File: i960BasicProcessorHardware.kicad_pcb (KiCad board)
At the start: 4 copper layers, 169.9 x 169.8 mm, 76 parts, among them J1 Conn_01x08, J10 Conn_02x39_Odd_Even, J11 Conn_01x03, J12 Conn_01x03, J13 AVR-ISP-6, J14 Conn_01x06 (Serial Connector), J15 Conn_01x01, J16 Conn_01x01, J2 Conn_02x05_Odd_Even, J3 Conn_02x05_Odd_Even, J4 Conn_02x05_Odd_Even, J5 Conn_02x16_Odd_Even, J6 Conn_01x03, J7 Conn_01x03, J8 Conn_01x06, J9 Conn_01x11, U1 74HC245, U10 Adafruit_FeatherWing (PSRAM F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, U11 Adafruit_FeatherWing (PSRAM F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, U12 74LS125, U13 74LS04, U14 74LS08, U15 74LS174, U16 SN74LVC245AN, U17 74LS174, U18 ATmega1284P-PU, U2 80960Sx, U3 MCP23S17_SP, U4 MCP23S17_SP, U5 74HC245, U6 74HC573, U7 74HC573, U8 MCP23S17_SP, U9 MCP23S17_SP

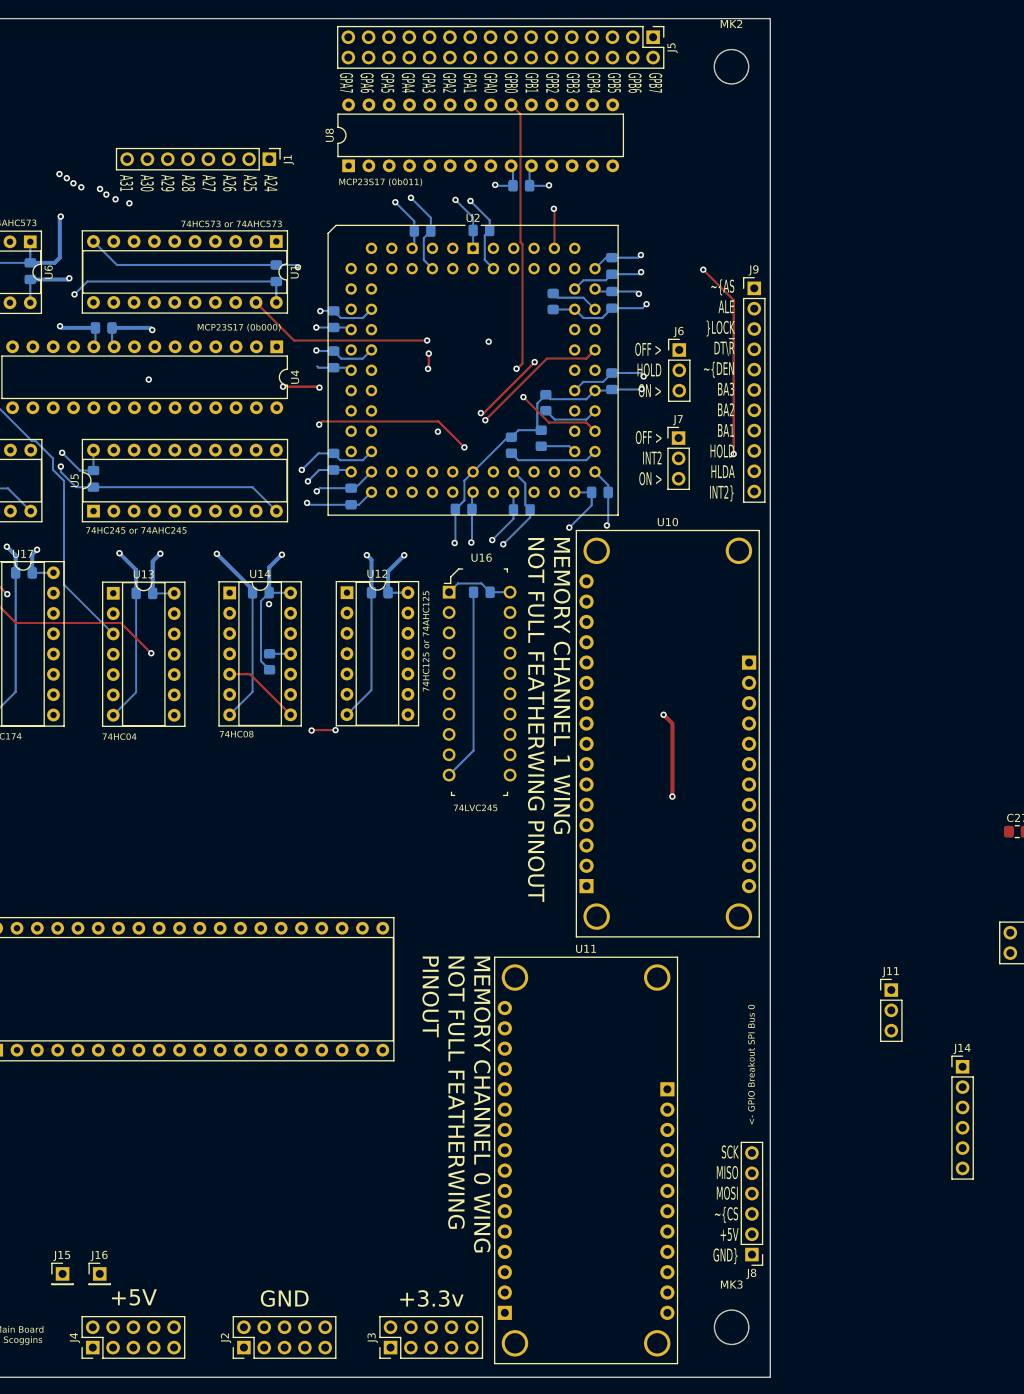
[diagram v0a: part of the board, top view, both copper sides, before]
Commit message: Add an onboard oscillator when it is necessary to program the secondary processor
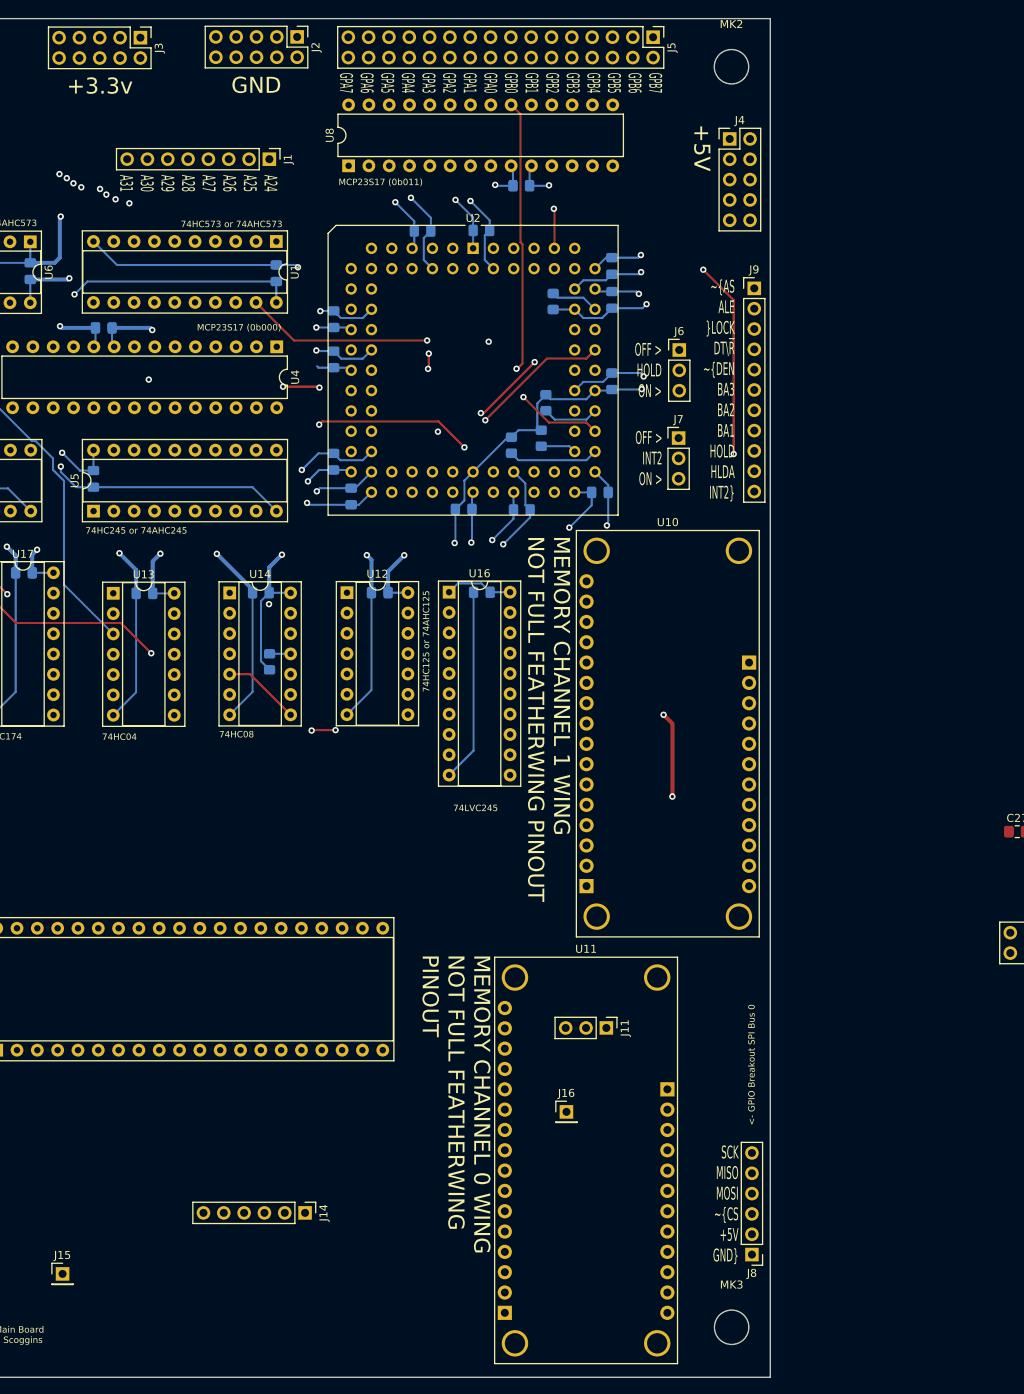
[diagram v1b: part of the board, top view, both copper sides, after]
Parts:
- U16: footprint digikey-footprints:DIP-20_W7.62mm -> Package_DIP:DIP-20_W7.62mm_Socket
- moved J4 170.8 mm to (181.8, 45.0), turned to 0 degrees
- moved J3 166.7 mm to (108.1, 32.4), turned to 270 degrees
- moved J2 164.0 mm to (127.7, 32.3), turned to 270 degrees
- moved J14 84.2 mm to (128.7, 179.3), turned to 270 degrees
- moved J16 61.8 mm to (161.4, 166.7)
- moved J11 35.9 mm to (166.4, 156.2), turned to 270 degrees

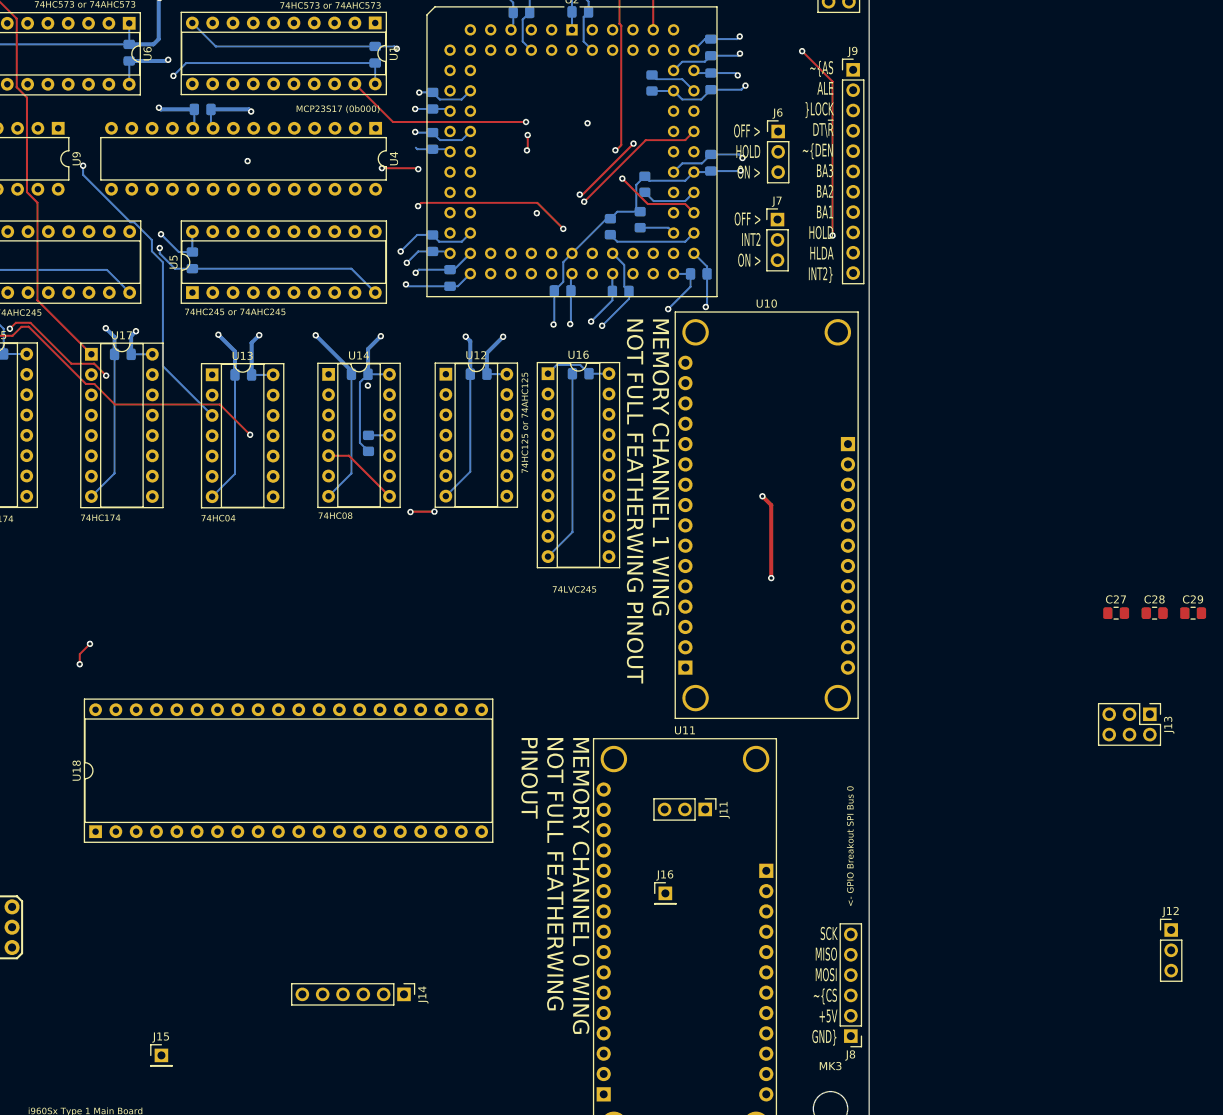
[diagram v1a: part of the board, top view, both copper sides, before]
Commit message: Move the coprocessor clock source selector to the main page
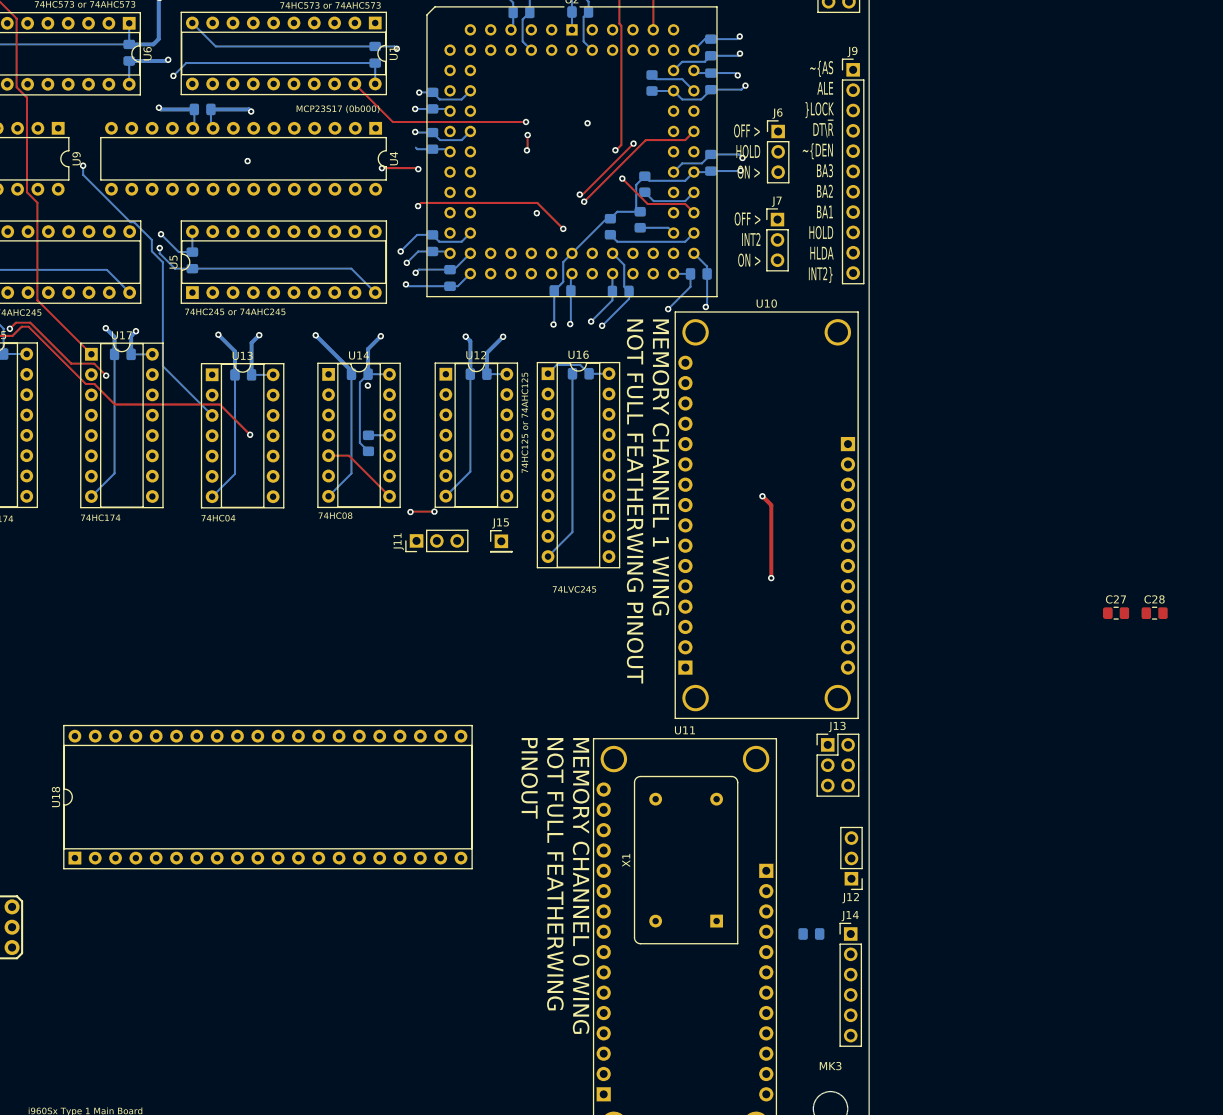
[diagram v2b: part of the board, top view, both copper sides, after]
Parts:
- removed J16: Conn_01x01, Connector_PinHeader_2.54mm:PinHeader_1x01_P2.54mm_Vertical
- removed J8: Conn_01x06, Connector_PinHeader_2.54mm:PinHeader_1x06_P2.54mm_Vertical
- added X1: CXO_DIP14, Oscillator:Oscillator_DIP-14, F.Cu at (167.8, 170.1)
- C29: moved to B.Cu
- moved J15 77.0 mm to (140.9, 122.6)
- moved C29 62.3 mm to (179.6, 171.7), turned to 180 degrees
- moved J14 56.4 mm to (184.5, 171.7), turned to 0 degrees
- moved J11 49.3 mm to (130.3, 122.6), turned to 90 degrees
- moved J12 40.5 mm to (184.6, 164.8), turned to 180 degrees
- moved J13 40.4 mm to (181.7, 148.1), turned to 0 degrees
- moved U18 4.19 mm to (87.6, 162.2)
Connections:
- J11 pad 3: /Sheet7D8CCC79/PCLK -> /PCLK
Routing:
- net /~GPIO_CS: track 366.9 -> 219.8 mm, vias 3 -> 1
- net /~3V_PSRAM_EN1: track 60.4 -> 0.00 mm
- net /~3V_PSRAM_EN2: track 59.8 -> 0.00 mm
- net /MOSI0: track 310.3 -> 254.0 mm
- net /SCK0: track 309.3 -> 253.3 mm, vias 4 -> 2
- net /MOSI1: track 110.7 -> 64.2 mm
- net /SCK1: track 107.7 -> 63.3 mm
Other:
- board text removed: "<- GPIO Breakout SPI Bus 0"
- board text removed: "SCK MISO MOSI ~CS +5V GND"

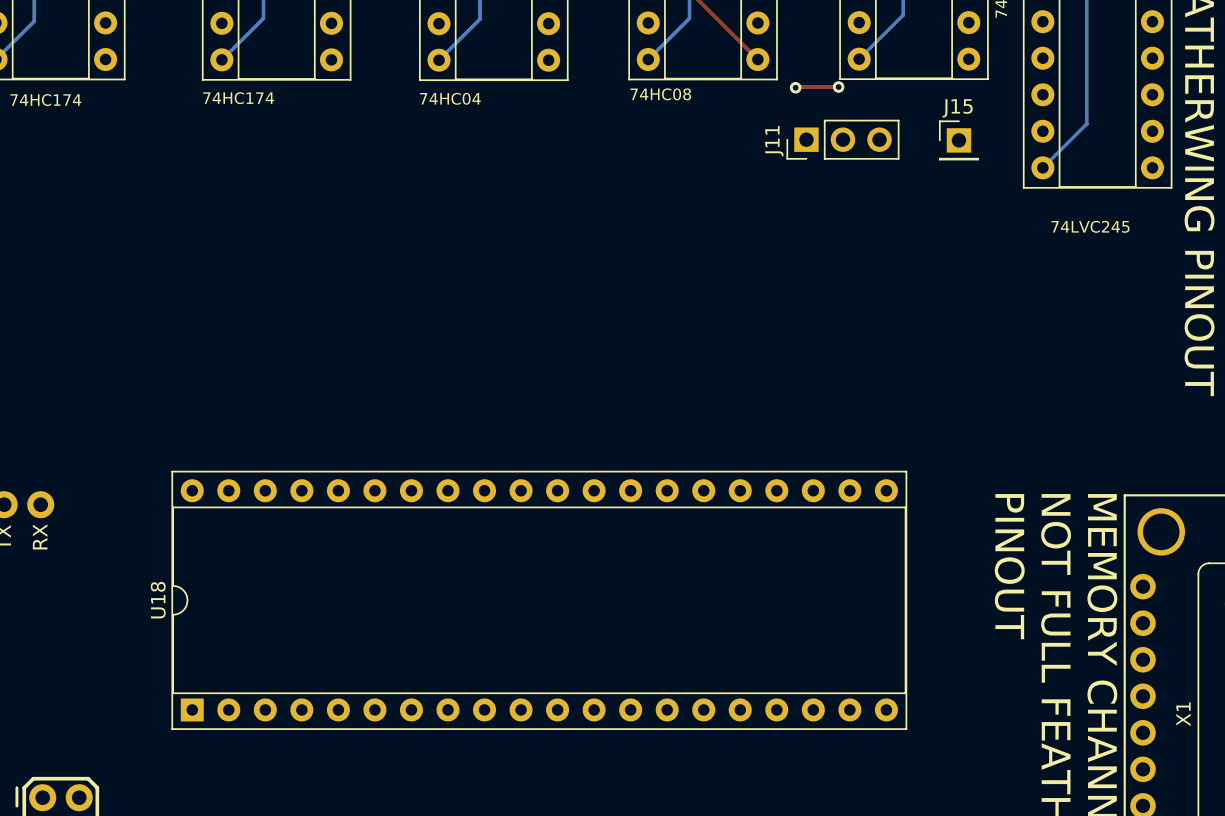
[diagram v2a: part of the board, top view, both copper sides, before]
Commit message: breakout all of the coprocessor0 pins to separate headers
Bundle the AREF pin with PORTA
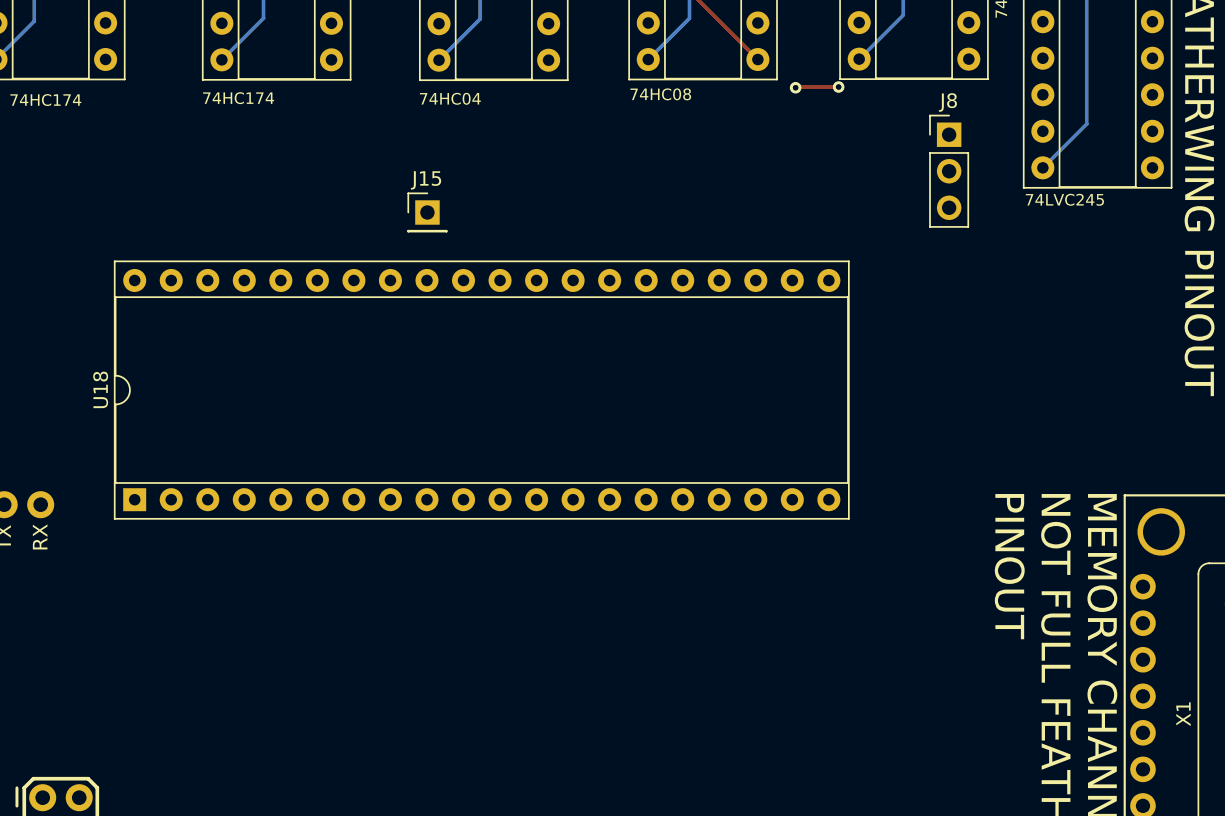
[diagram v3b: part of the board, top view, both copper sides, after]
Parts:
- removed J11: Conn_01x03, Connector_PinHeader_2.54mm:PinHeader_1x03_P2.54mm_Vertical
- added J8: Conn_01x03, Connector_PinHeader_2.54mm:PinHeader_1x03_P2.54mm_Vertical, F.Cu at (140.2, 122.2)
- moved J15 37.3 mm to (103.9, 127.7)
- moved U18 15.2 mm to (83.6, 147.6)
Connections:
- U18 pad 13: /Sheet7D8CCC79/EXTCLK -> /EXTCLK
